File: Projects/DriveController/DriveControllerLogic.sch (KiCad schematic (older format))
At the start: 41 parts, among them J1 HPCE_40-24, J2 ISP_Header, U1 ATMega32M1, U2 MCP2562, U3 ATA6844, U4 ACS710

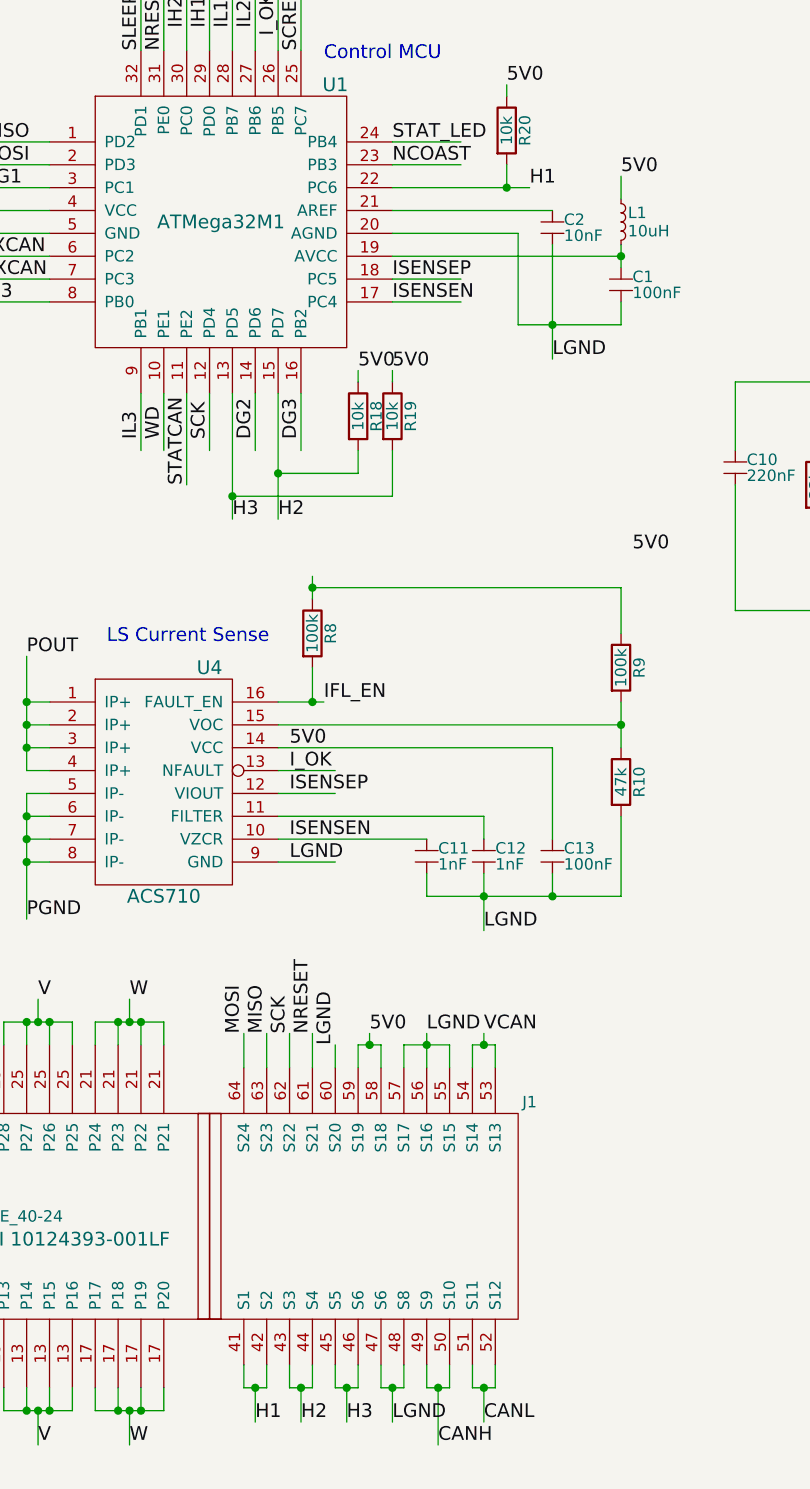
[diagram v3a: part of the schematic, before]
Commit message: Redone some routing - nearly finished!
There's a lot of room for improvement on the digital side.
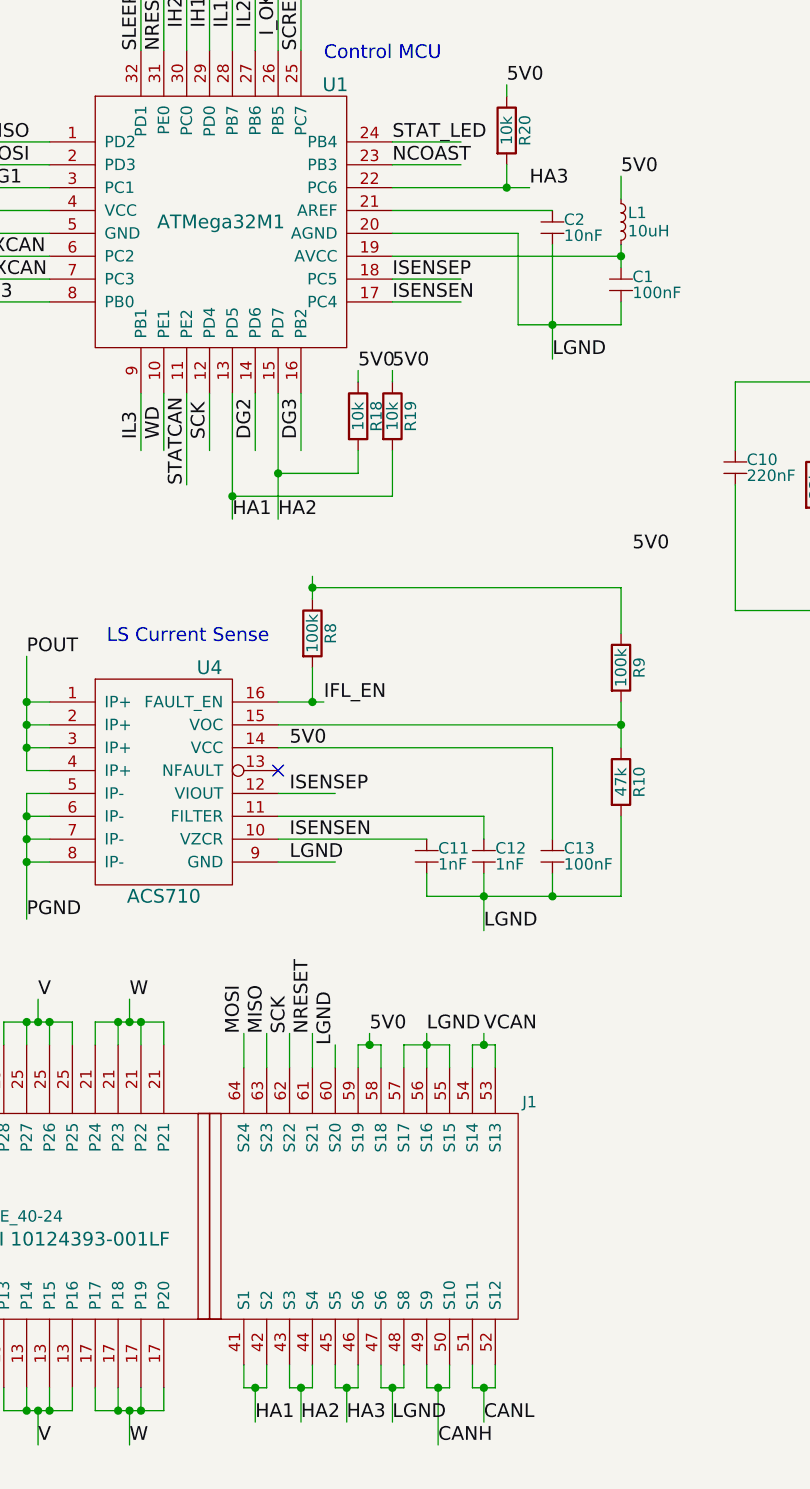
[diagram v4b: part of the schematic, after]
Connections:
- net labels added: HA1, HA2, HA3
- wire segments 299 -> 298
- no-connect marks 3 -> 4
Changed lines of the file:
@@
 ISENSEP
 Text Label 4250 3200 0    60   ~ 0
-H3
+HA1
 Text Label 4450 3200 0    60   ~ 0
-H2
+HA2
 Text Label 5550 1750 0    60   ~ 0
-H1
+HA3
 Text Label 3150 1750 0    60   ~ 0
 DG1
@@
 	1    0    0    -1
 $EndComp
-Text Label 4500 4300 0    60   ~ 0
-I_OK
 Text Label 4500 4400 0    60   ~ 0
 ISENSEP
@@
 CANH
 Text Label 4750 7150 0    60   ~ 0
-H3
+HA3
 Text Label 4550 7150 0    60   ~ 0
-H2
+HA2
 Text Label 4350 7150 0    60   ~ 0
-H1
+HA1
 Wire Wire Line
 	700  1850 1100 1850
@@
 	6450 3050 6450 3600
 Connection ~ 6800 3600
-Wire Wire Line
-	4450 4300 4700 4300
 Wire Wire Line
 	4450 4400 4700 4400
@@
 	1    0    0    -1
 $EndComp
+NoConn ~ 4450 4300
 $EndSCHEMATC

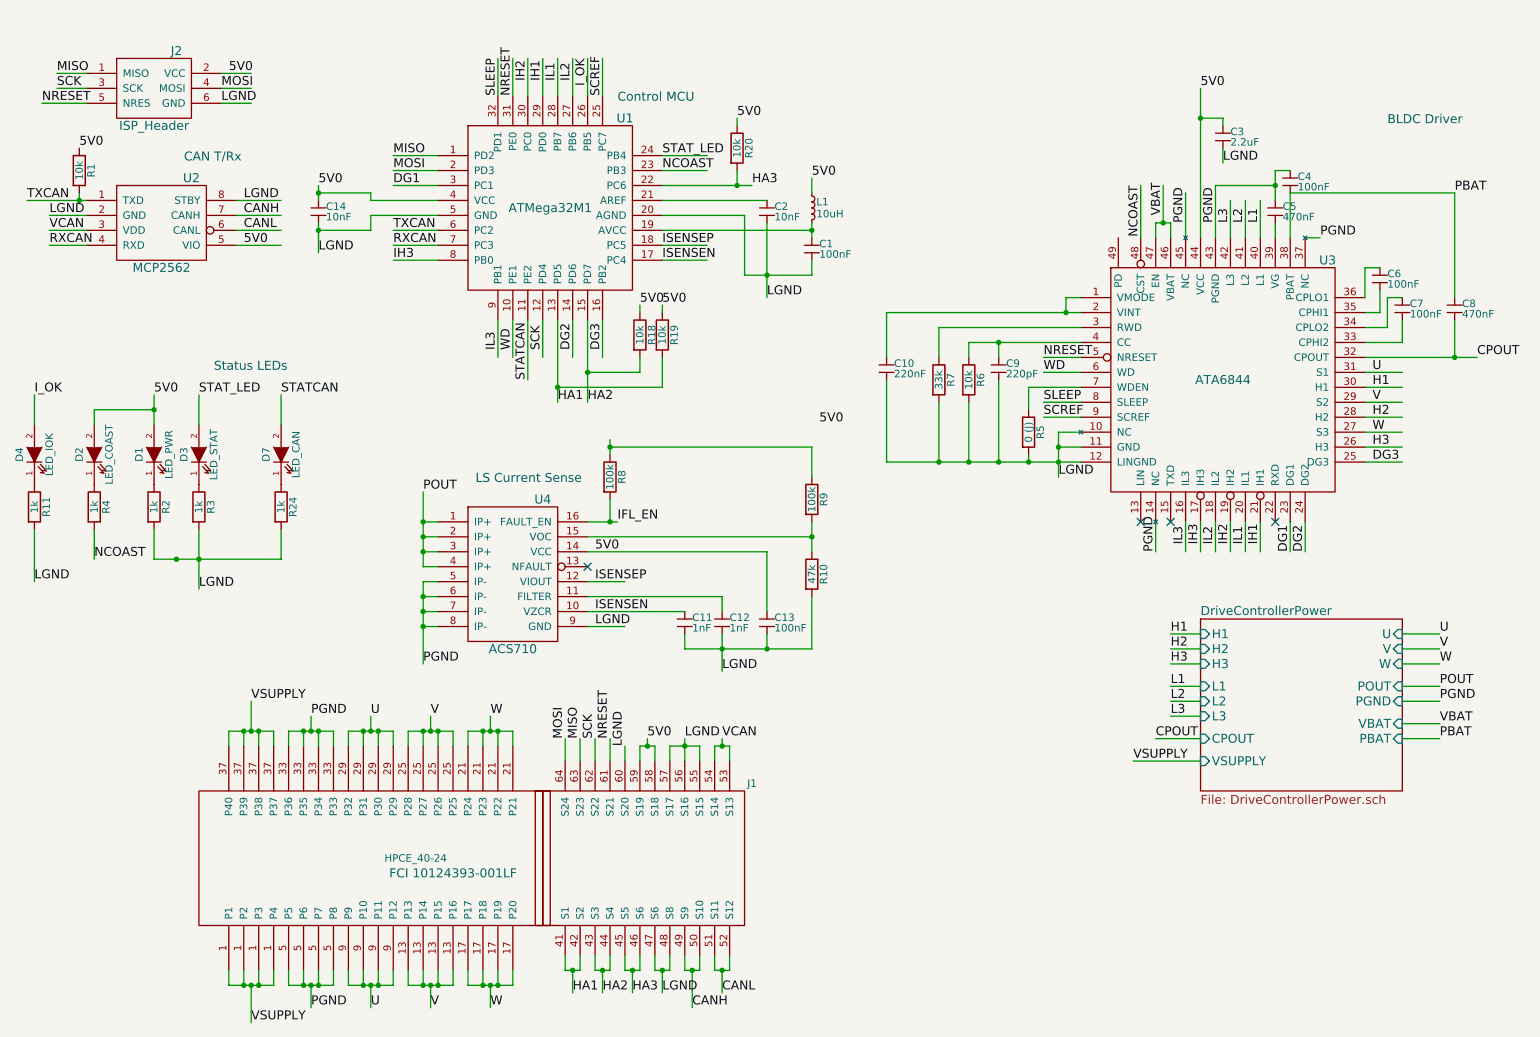
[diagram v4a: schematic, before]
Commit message: More PCB layout cleaning for Drive PCB
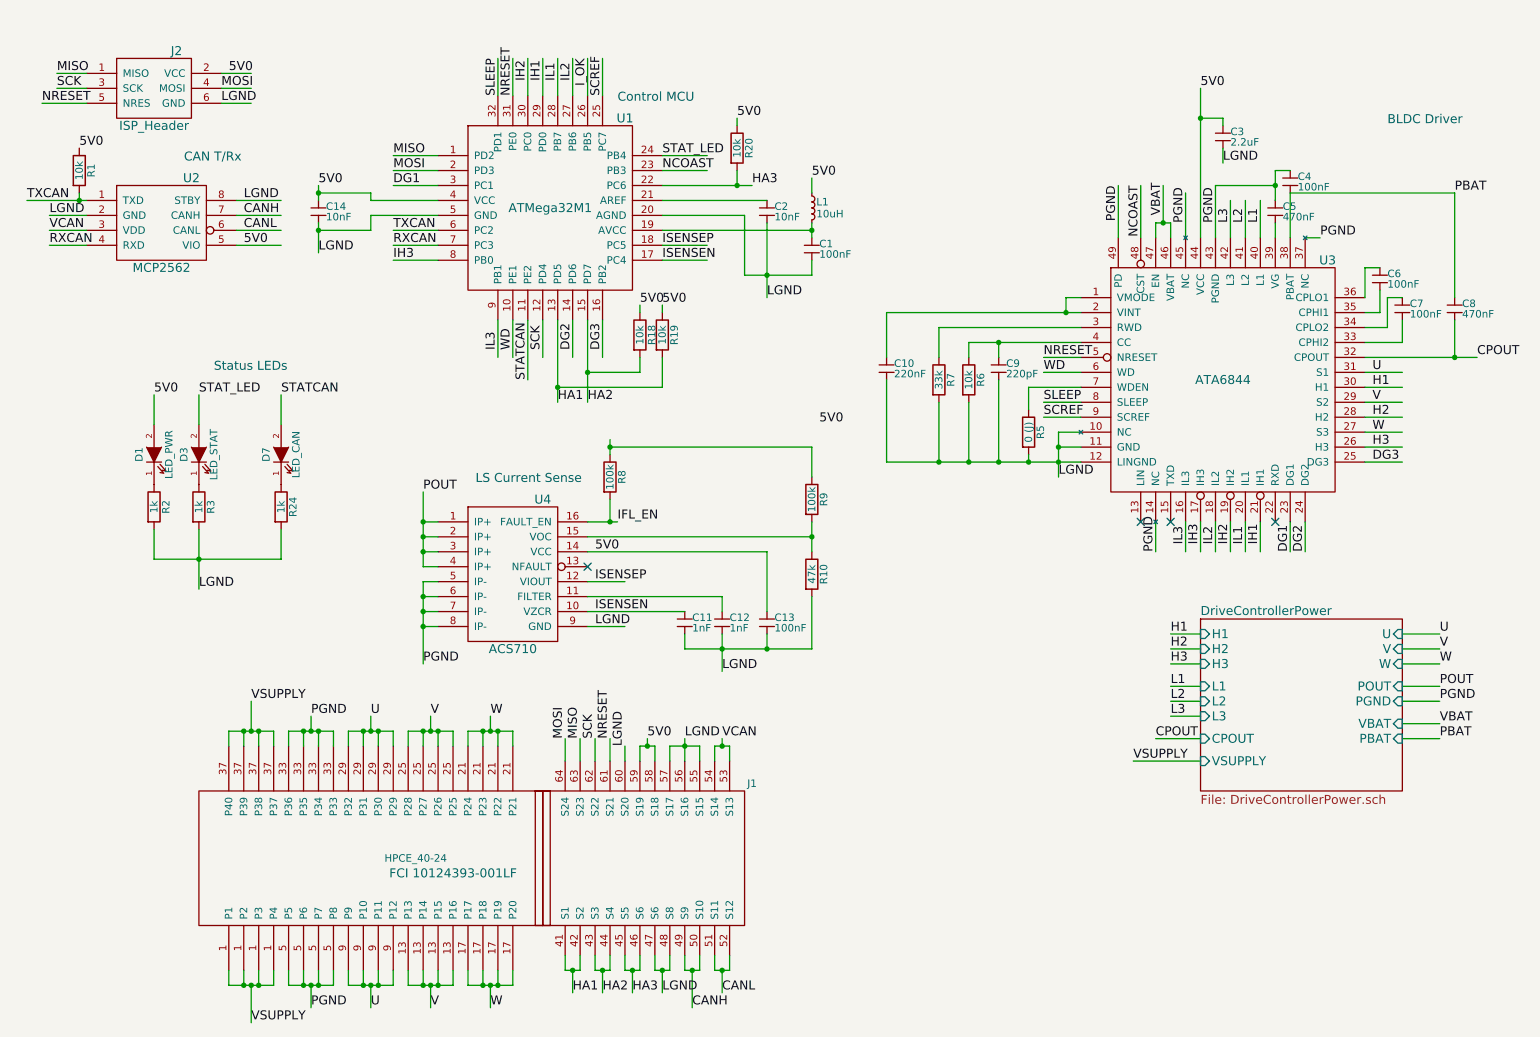
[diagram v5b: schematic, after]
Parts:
- removed D2: LED_COAST, LEDs:LED-0805, symbol LED
- removed D4: LED_IOK, LEDs:LED-0805, symbol LED
- removed R11, R4: 1k, Resistors_SMD:R_0805, symbol R
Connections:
- wire segments 298 -> 294
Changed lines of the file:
@@
 Text Notes 1950 3000 0    60   ~ 0
 Status LEDs
-$Comp
-L R R4
-U 1 1 56444C3B
-P 1150 3900
-F 0 "R4" V 1230 3900 50  0000 C CNN
-F 1 "1k" V 1150 3900 50  0000 C CNN
-F 2 "Resistors_SMD:R_0805" V 1080 3900 30  0001 C CNN
-F 3 "" H 1150 3900 30  0000 C CNN
-	1    1150 3900
-	1    0    0    -1
-$EndComp
-$Comp
-L LED D2
-U 1 1 56444C91
-P 1150 3550
-F 0 "D2" H 1150 3650 50  0000 C CNN
-F 1 "LED_COAST" H 1150 3450 50  0000 C CNN
-F 2 "LEDs:LED-0805" H 1150 3550 60  0001 C CNN
-F 3 "" H 1150 3550 60  0000 C CNN
-	1    1150 3550
-	0    -1   -1   0
-$EndComp
-Text Label 1150 4250 0    60   ~ 0
-NCOAST
 Text Label 8150 1750 3    60   ~ 0
 NCOAST
@@
 	1    0    0    -1
 $EndComp
-$Comp
-L LED D4
-U 1 1 5645E262
-P 750 3550
-F 0 "D4" H 750 3650 50  0000 C CNN
-F 1 "LED_IOK" H 750 3450 50  0000 C CNN
-F 2 "LEDs:LED-0805" H 750 3550 60  0001 C CNN
-F 3 "" H 750 3550 60  0000 C CNN
-	1    750  3550
-	0    -1   -1   0
-$EndComp
-$Comp
-L R R11
-U 1 1 5645E5E5
-P 750 3900
-F 0 "R11" V 830 3900 50  0000 C CNN
-F 1 "1k" V 750 3900 50  0000 C CNN
-F 2 "Resistors_SMD:R_0805" V 680 3900 30  0001 C CNN
-F 3 "" H 750 3900 30  0000 C CNN
-	1    750  3900
-	1    0    0    -1
-$EndComp
-Text Label 750  3150 0    60   ~ 0
-I_OK
 Text Label 10150 4750 0    60   ~ 0
 U
@@
 Wire Wire Line
 	1550 4250 2400 4250
-Connection ~ 1700 4250
-Wire Wire Line
-	1150 3350 1150 3250
-Wire Wire Line
-	1150 3250 1550 3250
-Connection ~ 1550 3250
-Wire Wire Line
-	1150 4050 1150 4250
 Wire Wire Line
 	8150 1750 8150 2100
@@
 	5950 3500 5950 3700
 Connection ~ 4600 3500
-Wire Wire Line
-	750  3350 750  3150
-Wire Wire Line
-	750  4050 750  4400
 Wire Wire Line
 	9900 4750 10150 4750
@@
 Wire Wire Line
 	5300 5500 5300 5600
-Text Label 750  4400 0    60   ~ 0
-LGND
 $Comp
 L HPCE_40-24 J1
@@
 $EndComp
 NoConn ~ 4450 4300
+Wire Wire Line
+	8000 1750 8000 2100
+Text Label 8000 1750 3    60   ~ 0
+PGND
 $EndSCHEMATC
